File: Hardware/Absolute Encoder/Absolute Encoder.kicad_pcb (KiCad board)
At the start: 2 copper layers, 130 x 30 mm, 16 parts, among them J1 Conn_01x05, U1 74LS165, U2 74LS165

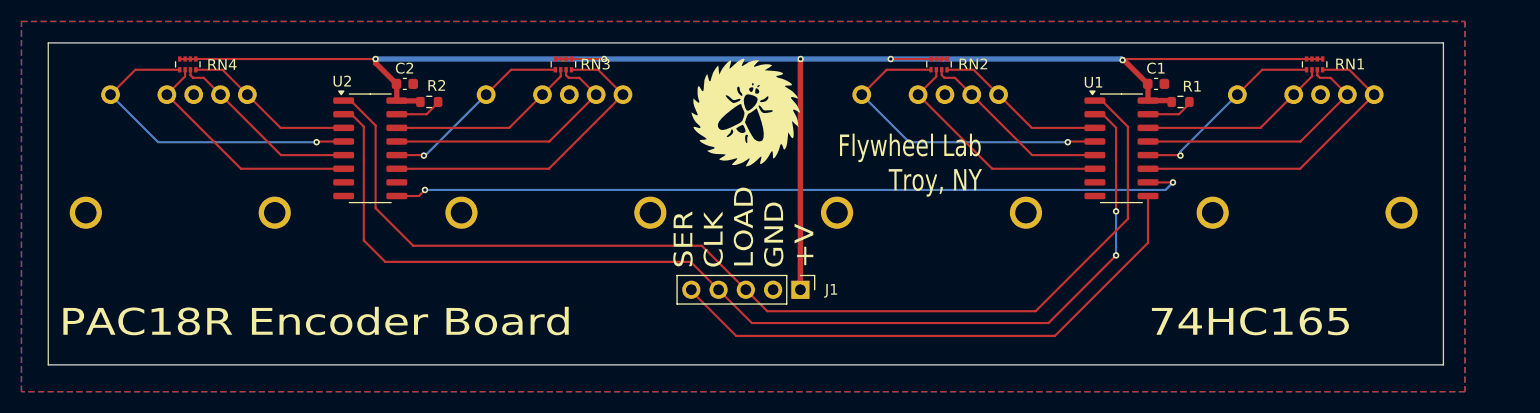
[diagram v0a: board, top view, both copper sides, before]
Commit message: Added mount holes
First draft of the silk
Mount Holes
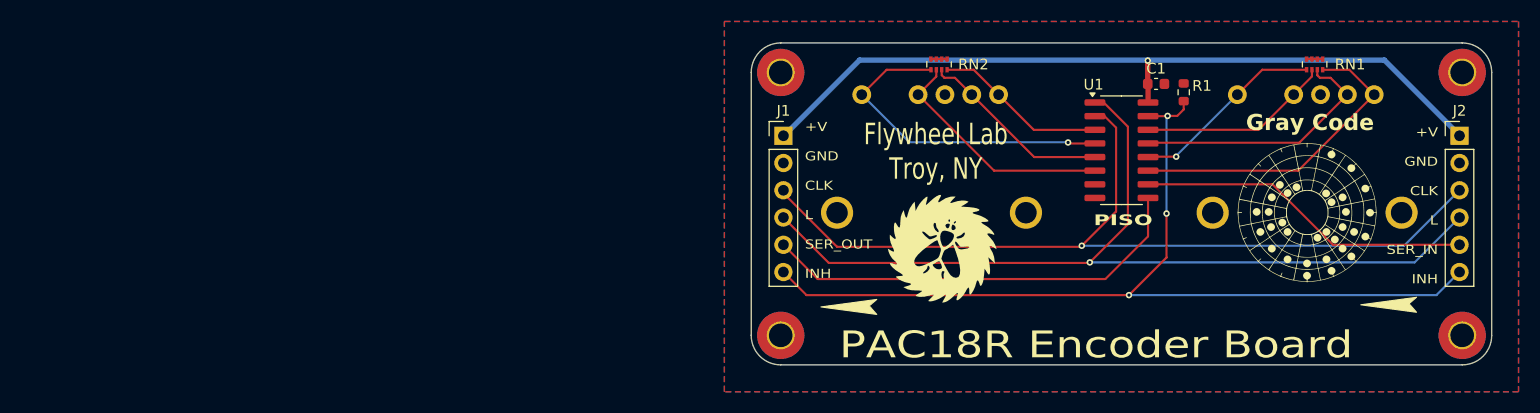
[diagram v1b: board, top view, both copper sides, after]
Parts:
- removed C2: 0.1uF, Capacitor_SMD:C_0603_1608Metric
- removed R2: 10K, Resistor_SMD:R_0603_1608Metric
- removed RN3, RN4: 10K, Resistor_SMD:R_Array_Concave_4x0402
- removed S3, S4: ~, Flywheel:PAC18R
- removed U2: 74LS165, Package_SO:SOIC-16_3.9x9.9mm_P1.27mm
- added G***: LOGO, Flywheel:GrayCodeWheel, F.Cu at (221.8, 75.8)
- added H1: Mount PTH, MountingHole:MountingHole_2.2mm_M2_Pad_TopBottom, F.Cu at (236.2, 87.2)
- added H2: Mount PTH, MountingHole:MountingHole_2.2mm_M2_Pad_TopBottom, F.Cu at (236.2, 62.8)
- added H3: Mount PTH, MountingHole:MountingHole_2.2mm_M2_Pad_TopBottom, F.Cu at (172.8, 87.2)
- added H4: Mount PTH, MountingHole:MountingHole_2.2mm_M2_Pad_TopBottom, F.Cu at (172.8, 62.8)
- added J2: PISO_IN, Connector_PinHeader_2.54mm:PinHeader_1x06_P2.54mm_Vertical, F.Cu at (236.0, 68.7)
- J1: value Conn_01x05 -> PISO_OUT; footprint Connector_PinHeader_2.54mm:PinHeader_1x05_P2.54mm_Vertical -> Connector_PinHeader_2.54mm:PinHeader_1x06_P2.54mm_Vertical
- R1: value 10K -> 100K
- moved G*** 22.3 mm to (187.8, 79.2)
- moved J1 14.4 mm to (173.0, 68.7), turned to 0 degrees
- moved R1 0.95 mm to (210.3, 64.6), turned to -90 degrees
- moved U1 0.18 mm to (204.5, 70.0)
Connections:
- C1 pad 1: +5V -> VDD
- J1 pad 1: +5V -> VDD
- J1 pad 3: /LOAD -> /CLK
- J1 pad 4: /CLK -> /LOAD
- R1 pad 1: +5V -> GND
- R1 pad 2: Net-(U1-~{CE}) -> /INH
- RN1 pad 5: +5V -> GND
- RN1 pad 6: +5V -> GND
- RN1 pad 7: +5V -> GND
- RN1 pad 8: +5V -> GND
- RN2 pad 5: +5V -> GND
- RN2 pad 6: +5V -> GND
- RN2 pad 7: +5V -> GND
- RN2 pad 8: +5V -> GND
- U1 pad 10: /CASCADE -> /SER_IN
- U1 pad 15: Net-(U1-~{CE}) -> /INH
- U1 pad 16: +5V -> VDD
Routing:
- net +5V: track 151.9 -> 0.00 mm, vias 5 -> 0
- net /INH: track 0.00 -> 87.3 mm, vias 0 -> 3
- net /CASCADE: track 75.2 -> 0.00 mm, vias 2 -> 0
- net VDD: track 0.00 -> 72.8 mm, vias 0 -> 1
- net /SER_IN: track 0.00 -> 31.4 mm
- net Net-(RN4-R1.1): track 31.0 -> 0.00 mm, vias 1 -> 0
- net Net-(RN3-R4.1): track 29.7 -> 0.00 mm
- net Net-(RN3-R3.1): track 24.4 -> 0.00 mm
- net Net-(RN4-R2.1): track 22.4 -> 0.00 mm
- net /CLK: track 103.2 -> 82.3 mm, vias 2 -> 1
- net Net-(RN3-R1.1): track 18.1 -> 0.00 mm, vias 1 -> 0
- net Net-(RN3-R2.1): track 17.9 -> 0.00 mm
- net Net-(RN4-R3.1): track 17.9 -> 0.00 mm
- net /LOAD: track 102.0 -> 84.6 mm, vias 0 -> 1
- net Net-(RN4-R4.1): track 16.0 -> 0.00 mm
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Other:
- board size 130 x 30 mm -> 69 x 30 mm
- board text added: "+V GD CL L IN IH"
- board text added: "+V GD CL L OUT IH"
- board text added: "+V GND CLK L SER_IN INH"
- board text added: "+V GND CLK L SER_OUT INH"
- board text added: "Gray Code"
- board text added: "PISO"
- board text removed: "74HC165"
- board text removed: "SER CLK LOAD GND +V"
